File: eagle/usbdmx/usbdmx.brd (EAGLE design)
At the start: 63.2 x 50.2 mm, 33 parts, among them IC1 MAX3468CSA, IC2 MAX3468CSA, Q1 16MHz

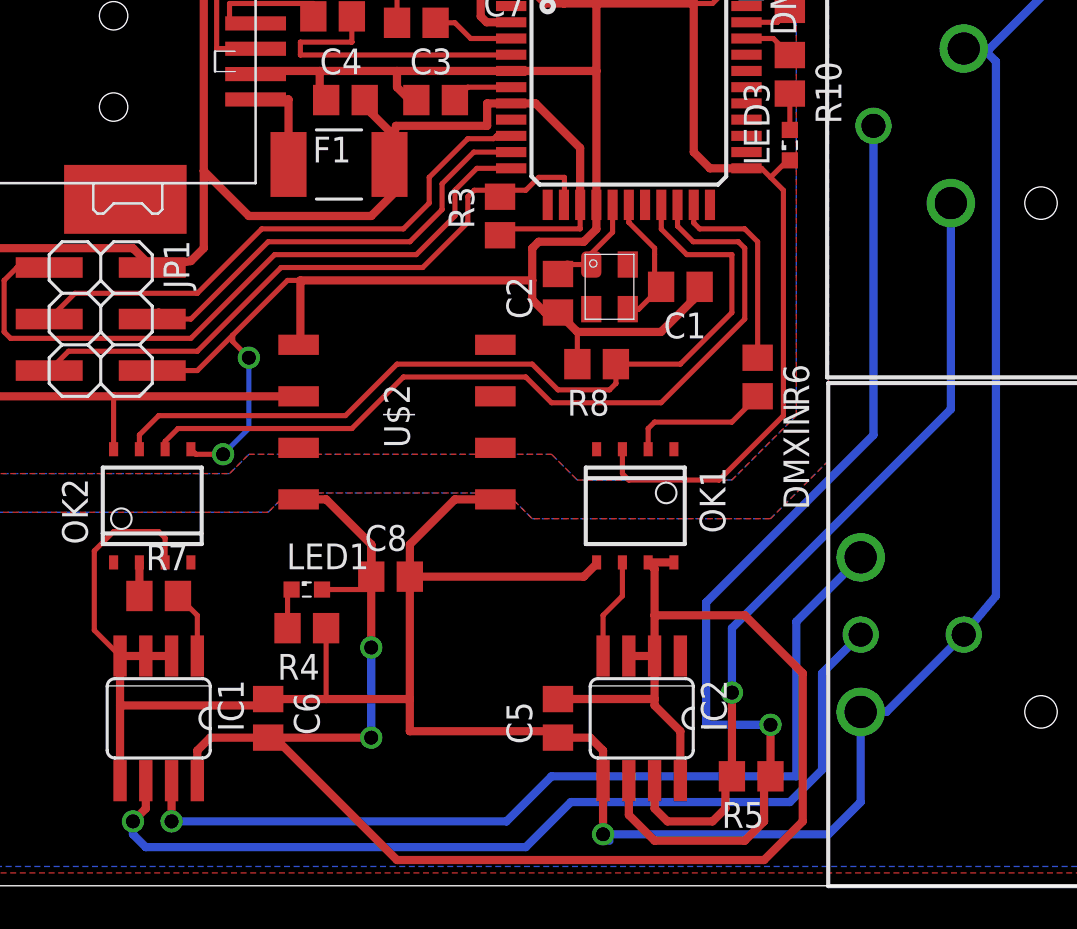
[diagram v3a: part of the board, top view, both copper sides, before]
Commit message: invert outputs due to optocoupler
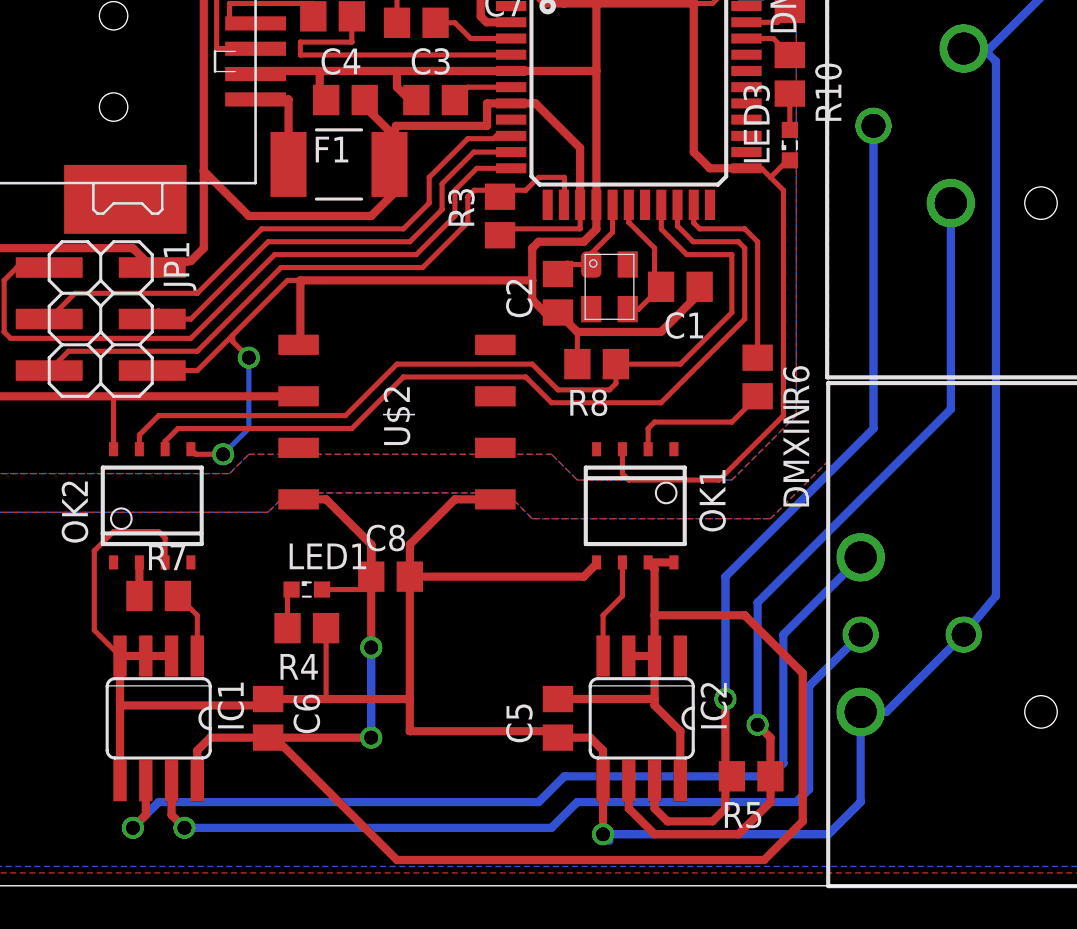
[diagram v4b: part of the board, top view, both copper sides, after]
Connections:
- removed net N$19: DMXIN.2, IC1.7
- new net N$29: DMXIN.3, IC1.7
- net N$12: now also DMXOUT.2; no longer DMXOUT.3
- net N$17: now also DMXOUT.3; no longer DMXOUT.2
- net N$18: now also DMXIN.2; no longer DMXIN.3
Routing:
- net N$19: track 45.8 -> 0.00 mm, vias 1 -> 0
- net N$29: track 0.00 -> 42.8 mm, vias 0 -> 1
- net N$12: track 50.3 -> 43.3 mm
- net N$17: track 39.8 -> 42.3 mm
- net N$18: track 46.2 -> 47.7 mm
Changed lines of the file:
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@@
 </signal>
 <signal name="N$17">
-<contactref element="DMXOUT" pad="2"/>
-<contactref element="R5" pad="2"/>
 <contactref element="IC2" pad="7"/>
 <wire x1="35.2425" y1="5.1816" x2="35.2425" y2="3.81" width="0.4064" layer="1"/>
 <wire x1="35.2425" y1="3.81" x2="35.8775" y2="3.175" width="0.4064" layer="1"/>
 <wire x1="35.8775" y1="3.175" x2="38.1" y2="3.175" width="0.4064" layer="1"/>
+<contactref element="DMXOUT" pad="3"/>
+<contactref element="R5" pad="2"/>
+<via x="38.735" y="9.2075" extent="1-16" drill="0.7" shape="square"/>
+<wire x1="38.735" y1="9.2075" x2="38.735" y2="15.24" width="0.4064" layer="16"/>
+<wire x1="38.735" y1="15.24" x2="46.0375" y2="22.5425" width="0.4064" layer="16"/>
+<wire x1="46.0375" y1="22.5425" x2="46.0375" y2="37.46" width="0.4064" layer="16"/>
+<wire x1="46.0375" y1="37.46" x2="46.0325" y2="37.465" width="0.4064" layer="16"/>
 <wire x1="38.1" y1="3.175" x2="38.735" y2="3.81" width="0.4064" layer="1"/>
 <wire x1="38.735" y1="3.81" x2="38.735" y2="5.0775" width="0.4064" layer="1"/>
 <wire x1="38.735" y1="5.0775" x2="39.055" y2="5.3975" width="0.4064" layer="1"/>
-<wire x1="39.055" y1="5.3975" x2="39.055" y2="9.525" width="0.4064" layer="1"/>
-<wire x1="49.8475" y1="23.495" x2="49.8475" y2="33.655" width="0.4064" layer="16"/>
-<via x="39.055" y="9.525" extent="1-16" drill="0.7" shape="square"/>
-<wire x1="39.055" y1="9.525" x2="39.055" y2="12.7025" width="0.4064" layer="16"/>
-<wire x1="39.055" y1="12.7025" x2="49.8475" y2="23.495" width="0.4064" layer="16"/>
-</signal>
-<signal name="N$18">
-<contactref element="DMXIN" pad="3"/>
-<contactref element="IC1" pad="6"/>
-<wire x1="10.16" y1="5.1816" x2="10.16" y2="3.81" width="0.4064" layer="1"/>
-<wire x1="10.16" y1="3.81" x2="9.525" y2="3.175" width="0.4064" layer="1"/>
-<via x="9.525" y="3.175" extent="1-16" drill="0.7" shape="square"/>
-<wire x1="9.525" y1="3.175" x2="9.525" y2="2.54" width="0.4064" layer="16"/>
-<wire x1="9.525" y1="2.54" x2="10.16" y2="1.905" width="0.4064" layer="16"/>
-<wire x1="10.16" y1="1.905" x2="28.8925" y2="1.905" width="0.4064" layer="16"/>
-<wire x1="28.8925" y1="1.905" x2="31.115" y2="4.1275" width="0.4064" layer="16"/>
-<wire x1="45.4025" y1="12.3825" x2="43.4975" y2="10.4775" width="0.4064" layer="16"/>
-<wire x1="43.4975" y1="10.4775" x2="43.4975" y2="5.715" width="0.4064" layer="16"/>
-<wire x1="43.4975" y1="5.715" x2="41.91" y2="4.1275" width="0.4064" layer="16"/>
-<wire x1="41.91" y1="4.1275" x2="31.115" y2="4.1275" width="0.4064" layer="16"/>
-</signal>
-<signal name="N$19">
-<contactref element="IC1" pad="7"/>
-<contactref element="DMXIN" pad="2"/>
-<wire x1="11.43" y1="5.1816" x2="11.43" y2="3.175" width="0.4064" layer="1"/>
-<via x="11.43" y="3.175" extent="1-16" drill="0.7" shape="square"/>
-<wire x1="11.43" y1="3.175" x2="27.94" y2="3.175" width="0.4064" layer="16"/>
-<wire x1="27.94" y1="3.175" x2="30.1625" y2="5.3975" width="0.4064" layer="16"/>
-<wire x1="45.4025" y1="16.1925" x2="42.2275" y2="13.0175" width="0.4064" layer="16"/>
-<wire x1="42.2275" y1="13.0175" x2="42.2275" y2="5.3975" width="0.4064" layer="16"/>
-<wire x1="42.2275" y1="5.3975" x2="30.1625" y2="5.3975" width="0.4064" layer="16"/>
+<wire x1="39.055" y1="5.3975" x2="38.735" y2="5.7175" width="0.4064" layer="1"/>
+<wire x1="38.735" y1="5.7175" x2="38.735" y2="9.2075" width="0.4064" layer="1"/>
 </signal>
 <signal name="SVCC">
@@
 </signal>
 <signal name="N$12">
+<contactref element="DMXOUT" pad="2"/>
 <contactref element="IC2" pad="6"/>
 <contactref element="R5" pad="1"/>
-<contactref element="DMXOUT" pad="3"/>
-<wire x1="33.9725" y1="5.1816" x2="33.9725" y2="3.4925" width="0.4064" layer="1"/>
-<wire x1="33.9725" y1="3.4925" x2="35.2425" y2="2.2225" width="0.4064" layer="1"/>
-<wire x1="35.2425" y1="2.2225" x2="39.6875" y2="2.2225" width="0.4064" layer="1"/>
-<wire x1="39.6875" y1="2.2225" x2="40.64" y2="3.175" width="0.4064" layer="1"/>
-<wire x1="40.64" y1="3.175" x2="40.64" y2="5.0825" width="0.4064" layer="1"/>
-<wire x1="40.64" y1="5.0825" x2="40.955" y2="5.3975" width="0.4064" layer="1"/>
-<via x="40.9575" y="7.9375" extent="1-16" drill="0.7" shape="square"/>
-<wire x1="40.9575" y1="7.9375" x2="40.9575" y2="5.4" width="0.4064" layer="1"/>
-<wire x1="40.9575" y1="5.4" x2="40.955" y2="5.3975" width="0.4064" layer="1"/>
-<wire x1="46.0325" y1="22.22" x2="46.0325" y2="37.465" width="0.4064" layer="16"/>
-<wire x1="40.9575" y1="7.9375" x2="37.7825" y2="7.9375" width="0.4064" layer="16"/>
-<wire x1="37.7825" y1="7.9375" x2="37.7825" y2="13.97" width="0.4064" layer="16"/>
-<wire x1="37.7825" y1="13.97" x2="46.0325" y2="22.22" width="0.4064" layer="16"/>
+<wire x1="33.9725" y1="5.1816" x2="33.9725" y2="3.81" width="0.4064" layer="1"/>
+<wire x1="33.9725" y1="3.81" x2="35.2425" y2="2.54" width="0.4064" layer="1"/>
+<wire x1="35.2425" y1="2.54" x2="39.37" y2="2.54" width="0.4064" layer="1"/>
+<wire x1="39.37" y1="2.54" x2="40.9575" y2="4.1275" width="0.4064" layer="1"/>
+<wire x1="40.9575" y1="4.1275" x2="40.9575" y2="5.395" width="0.4064" layer="1"/>
+<wire x1="40.9575" y1="5.395" x2="40.955" y2="5.3975" width="0.4064" layer="1"/>
+<wire x1="40.955" y1="5.3975" x2="40.955" y2="7.305" width="0.4064" layer="1"/>
+<wire x1="40.955" y1="7.305" x2="40.3225" y2="7.9375" width="0.4064" layer="1"/>
+<via x="40.3225" y="7.9375" extent="1-16" drill="0.7" shape="square"/>
+<wire x1="40.3225" y1="7.9375" x2="40.3225" y2="13.97" width="0.4064" layer="16"/>
+<wire x1="40.3225" y1="13.97" x2="49.8475" y2="23.495" width="0.4064" layer="16"/>
+<wire x1="49.8475" y1="23.495" x2="49.8475" y2="33.655" width="0.4064" layer="16"/>
 </signal>
 <signal name="N$23">
@@
 <wire x1="41.095" y1="41.77" x2="41.91" y2="40.955" width="0.254" layer="1"/>
 </signal>
+<signal name="N$29">
+<contactref element="IC1" pad="7"/>
+<contactref element="DMXIN" pad="3"/>
+<wire x1="11.43" y1="5.1816" x2="11.43" y2="3.4925" width="0.4064" layer="1"/>
+<wire x1="11.43" y1="3.4925" x2="12.065" y2="2.8575" width="0.4064" layer="1"/>
+<via x="12.065" y="2.8575" extent="1-16" drill="0.7" shape="square"/>
+<wire x1="12.065" y1="2.8575" x2="30.1625" y2="2.8575" width="0.4064" layer="16"/>
+<wire x1="30.1625" y1="2.8575" x2="31.4325" y2="4.1275" width="0.4064" layer="16"/>
+<wire x1="31.4325" y1="4.1275" x2="42.2275" y2="4.1275" width="0.4064" layer="16"/>
+<wire x1="42.2275" y1="4.1275" x2="42.8625" y2="4.7625" width="0.4064" layer="16"/>
+<wire x1="42.8625" y1="4.7625" x2="42.8625" y2="9.8425" width="0.4064" layer="16"/>
+<wire x1="42.8625" y1="9.8425" x2="45.4025" y2="12.3825" width="0.4064" layer="16"/>
+</signal>
+<signal name="N$18">
+<contactref element="DMXIN" pad="2"/>
+<contactref element="IC1" pad="6"/>
+<wire x1="10.795" y1="4.1275" x2="29.5275" y2="4.1275" width="0.4064" layer="16"/>
+<wire x1="29.5275" y1="4.1275" x2="30.7975" y2="5.3975" width="0.4064" layer="16"/>
+<wire x1="10.16" y1="5.1816" x2="10.16" y2="3.4925" width="0.4064" layer="1"/>
+<wire x1="10.16" y1="3.4925" x2="9.525" y2="2.8575" width="0.4064" layer="1"/>
+<via x="9.525" y="2.8575" extent="1-16" drill="0.7" shape="square"/>
+<wire x1="9.525" y1="2.8575" x2="10.795" y2="4.1275" width="0.4064" layer="16"/>
+<wire x1="30.7975" y1="5.3975" x2="40.9575" y2="5.3975" width="0.4064" layer="16"/>
+<wire x1="40.9575" y1="5.3975" x2="41.5925" y2="6.0325" width="0.4064" layer="16"/>
+<wire x1="41.5925" y1="6.0325" x2="41.5925" y2="12.3825" width="0.4064" layer="16"/>
+<wire x1="41.5925" y1="12.3825" x2="45.4025" y2="16.1925" width="0.4064" layer="16"/>
+</signal>
 </signals>

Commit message: rewire
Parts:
- moved R1 0.32 mm to (23.5, 42.9)
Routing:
- net SVCC: track 92.5 -> 90.5 mm, vias 2 -> 0
- net SGND: vias 1 -> 3
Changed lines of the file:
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@@
 </element>
 <element name="Q1" library="Crystals-new" package="MT" value="16MHz" x="33.02" y="29.5275" rot="R270"/>
-<element name="R1" library="rcl" package="R0805" value="22" x="23.495" y="42.545"/>
+<element name="R1" library="rcl" package="R0805" value="22" x="23.495" y="42.8625"/>
 <element name="R2" library="rcl" package="R0805" value="22" x="19.3675" y="42.8625"/>
 <element name="R3" library="rcl" package="R0805" value="10k" x="27.6225" y="33.02" rot="R90"/>
@@
 <contactref element="U$1" pad="3"/>
 <wire x1="28.1725" y1="41.77" x2="26.175" y2="41.77" width="0.254" layer="1"/>
-<wire x1="26.175" y1="41.77" x2="25.4" y2="42.545" width="0.254" layer="1"/>
-<wire x1="25.4" y1="42.545" x2="24.445" y2="42.545" width="0.254" layer="1"/>
+<wire x1="26.175" y1="41.77" x2="25.0825" y2="42.8625" width="0.254" layer="1"/>
+<wire x1="25.0825" y1="42.8625" x2="24.445" y2="42.8625" width="0.254" layer="1"/>
 </signal>
 <signal name="N$4">
@@
 <wire x1="13.6525" y1="41.275" x2="13.6525" y2="44.1325" width="0.254" layer="1"/>
 <wire x1="22.545" y1="44.1325" x2="13.6525" y2="44.1325" width="0.254" layer="1"/>
-<wire x1="22.545" y1="44.1325" x2="22.545" y2="42.545" width="0.254" layer="1"/>
+<wire x1="22.545" y1="44.1325" x2="22.545" y2="42.8625" width="0.254" layer="1"/>
 </signal>
 <signal name="VCC">
@@
 <wire x1="12.7" y1="6.6675" x2="12.7" y2="5.1816" width="0.4064" layer="1"/>
 <wire x1="16.1925" y1="7.305" x2="16.5075" y2="7.305" width="0.4064" layer="1"/>
-<wire x1="16.5075" y1="7.305" x2="22.5425" y2="1.27" width="0.4064" layer="1"/>
 <wire x1="22.5425" y1="1.27" x2="40.64" y2="1.27" width="0.4064" layer="1"/>
 <wire x1="40.64" y1="1.27" x2="42.545" y2="3.175" width="0.4064" layer="1"/>
@@
 <wire x1="21.275" y1="15.24" x2="21.2725" y2="15.24" width="0.4064" layer="1"/>
 <wire x1="21.2725" y1="15.24" x2="21.2725" y2="14.605" width="0.4064" layer="1"/>
-<via x="21.2725" y="11.7475" extent="1-16" drill="0.7" shape="square"/>
-<wire x1="21.2725" y1="14.605" x2="21.2725" y2="11.7475" width="0.4064" layer="1"/>
-<wire x1="21.2725" y1="11.7475" x2="21.2725" y2="7.3025" width="0.4064" layer="16"/>
-<via x="21.2725" y="7.3025" extent="1-16" drill="0.7" shape="square"/>
 <wire x1="21.2725" y1="7.3025" x2="16.1925" y2="7.3025" width="0.4064" layer="1"/>
 <wire x1="16.1925" y1="7.3025" x2="16.1925" y2="7.305" width="0.4064" layer="1"/>
 <contactref element="LED1" pad="A"/>
 <wire x1="18.8475" y1="14.605" x2="21.2725" y2="14.605" width="0.254" layer="1"/>
+<wire x1="22.5425" y1="1.27" x2="21.2725" y2="2.54" width="0.4064" layer="1"/>
+<wire x1="21.2725" y1="2.54" x2="21.2725" y2="6.6675" width="0.4064" layer="1"/>
+<wire x1="21.2725" y1="6.6675" x2="21.2725" y2="7.3025" width="0.4064" layer="1"/>
+<wire x1="21.2725" y1="14.605" x2="21.2725" y2="7.3025" width="0.4064" layer="1"/>
 </signal>
 <signal name="SGND">
@@
 <wire x1="16.19" y1="9.205" x2="16.1925" y2="9.205" width="0.4064" layer="1"/>
 <wire x1="16.1925" y1="9.205" x2="19.05" y2="9.205" width="0.4064" layer="1"/>
-<wire x1="19.05" y1="9.205" x2="23.175" y2="9.205" width="0.4064" layer="1"/>
 <wire x1="45.4025" y1="8.5725" x2="45.4025" y2="4.1275" width="0.4064" layer="16"/>
 <wire x1="45.4025" y1="4.1275" x2="43.815" y2="2.54" width="0.4064" layer="16"/>
 <wire x1="43.815" y1="2.54" x2="32.7025" y2="2.54" width="0.4064" layer="16"/>
-<wire x1="23.175" y1="9.205" x2="23.175" y2="7.62" width="0.4064" layer="1"/>
 <contactref element="IC1" pad="2"/>
 <wire x1="10.16" y1="11.3284" x2="11.43" y2="11.3284" width="0.4064" layer="1"/>
@@
 <wire x1="23.1775" y1="16.8275" x2="23.1775" y2="15.2425" width="0.4064" layer="1"/>
 <wire x1="23.1775" y1="15.2425" x2="23.175" y2="15.24" width="0.4064" layer="1"/>
-<wire x1="23.175" y1="15.24" x2="23.175" y2="9.205" width="0.4064" layer="1"/>
+<wire x1="23.175" y1="15.24" x2="23.175" y2="9.2075" width="0.4064" layer="1"/>
+<wire x1="23.175" y1="8.89" x2="23.175" y2="7.62" width="0.4064" layer="1"/>
 <wire x1="31.75" y1="15.24" x2="23.175" y2="15.24" width="0.4064" layer="1"/>
+<via x="19.05" y="9.205" extent="1-16" drill="0.7" shape="square"/>
+<wire x1="19.05" y1="9.205" x2="19.0525" y2="9.2075" width="0.4064" layer="16"/>
+<wire x1="19.0525" y1="9.2075" x2="23.175" y2="9.2075" width="0.4064" layer="16"/>
+<via x="23.175" y="9.2075" extent="1-16" drill="0.7" shape="square"/>
+<wire x1="23.175" y1="9.2075" x2="23.175" y2="8.89" width="0.4064" layer="1"/>
 </signal>
 <signal name="N$20">

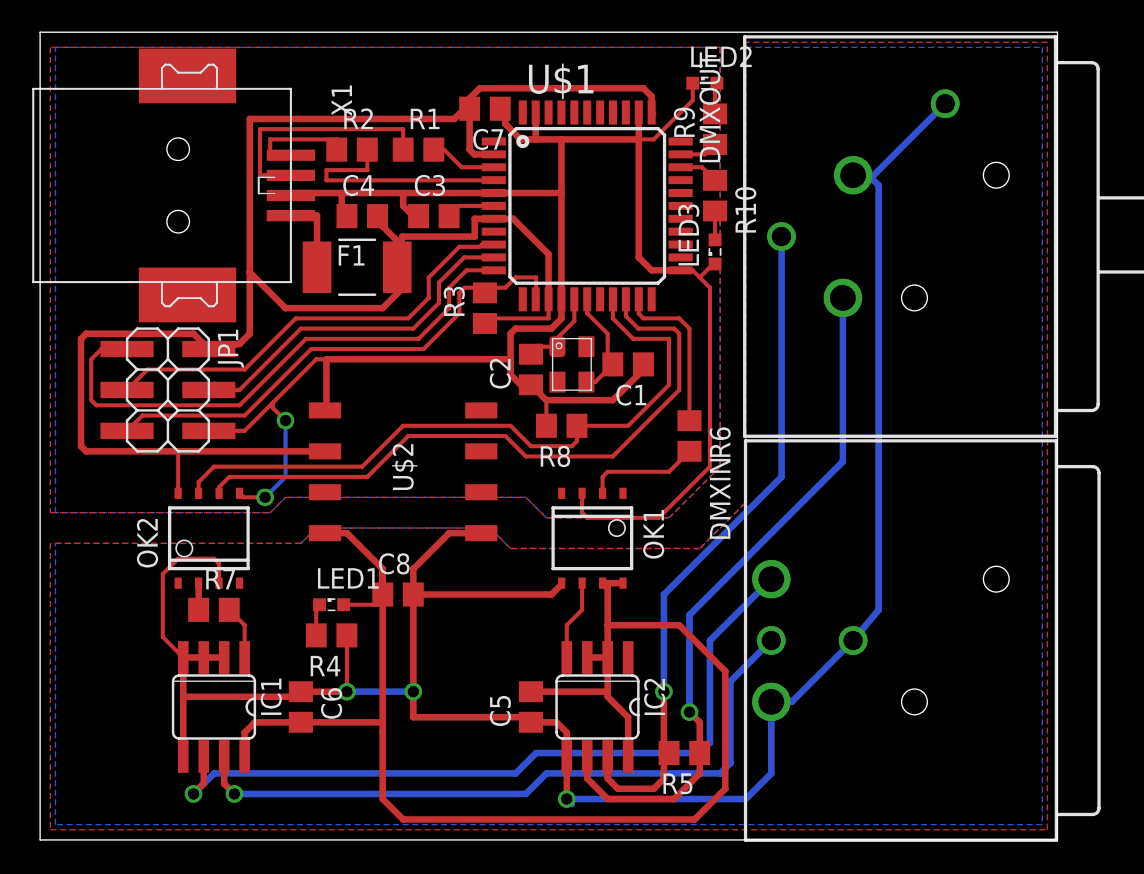
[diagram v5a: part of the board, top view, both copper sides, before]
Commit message: rewire some components to improve isolation
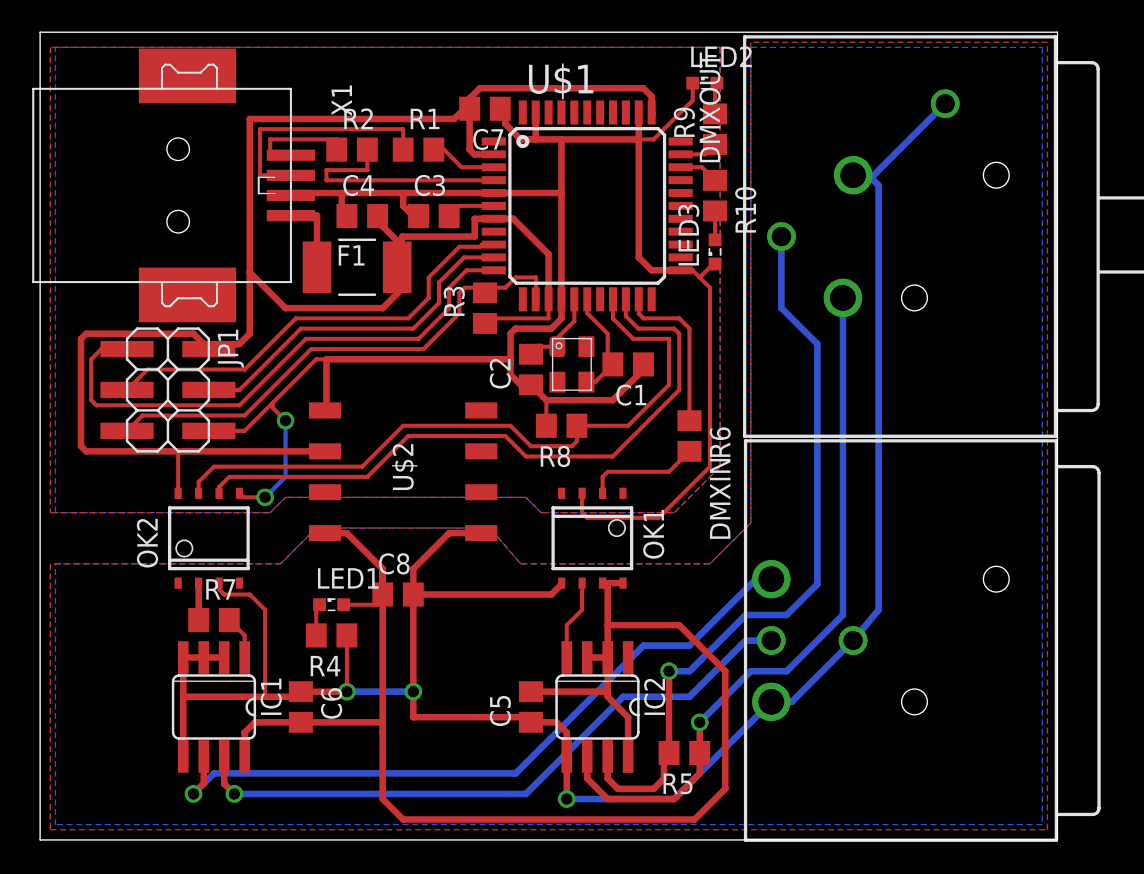
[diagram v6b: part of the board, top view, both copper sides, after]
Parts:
- moved R7 0.63 mm to (10.8, 13.7)
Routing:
- net SGND: track 137.7 -> 132.8 mm
- net N$17: track 42.3 -> 46.1 mm
- net N$18: track 47.7 -> 44.0 mm
- net N$29: track 42.8 -> 39.9 mm
- net N$12: track 43.3 -> 44.1 mm
- net N$21: track 3.35 -> 2.72 mm
- net N$23: track 1.66 -> 2.29 mm
